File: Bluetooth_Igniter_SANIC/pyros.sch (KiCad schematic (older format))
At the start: 21 parts, among them J1 Screw_Terminal_01x02, J2 Screw_Terminal_01x02, J3 Screw_Terminal_01x02, Q3 Q_NMOS_GSD, Q4 Q_NMOS_GSD, U3 LTV-817S, U4 LTV-817S

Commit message: PCB Resizing
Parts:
- J1, J2, J3: footprint TerminalBlock_Phoenix:TerminalBlock_Phoenix_PT-1,5-2-5.0-H_1x02_P5.00mm_Horizontal -> iclrhw:PHOENIX_1757242
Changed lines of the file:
@@
 F 0 "J1" V 2772 3630 50  0000 L CNN
 F 1 "Screw_Terminal_01x02" V 2863 3630 50  0000 L CNN
-F 2 "TerminalBlock_Phoenix:TerminalBlock_Phoenix_PT-1,5-2-5.0-H_1x02_P5.00mm_Horizontal" H 2900 3550 50  0001 C CNN
+F 2 "iclrhw:PHOENIX_1757242" H 2900 3550 50  0001 C CNN
 F 3 "~" H 2900 3550 50  0001 C CNN
 	1    2900 3550
@@
 F 0 "J3" V 7422 3680 50  0000 L CNN
 F 1 "Screw_Terminal_01x02" V 7513 3680 50  0000 L CNN
-F 2 "TerminalBlock_Phoenix:TerminalBlock_Phoenix_PT-1,5-2-5.0-H_1x02_P5.00mm_Horizontal" H 7550 3600 50  0001 C CNN
+F 2 "iclrhw:PHOENIX_1757242" H 7550 3600 50  0001 C CNN
 F 3 "~" H 7550 3600 50  0001 C CNN
 	1    7550 3600
@@
 F 0 "J2" H 3480 1692 50  0000 L CNN
 F 1 "Screw_Terminal_01x02" H 3480 1601 50  0000 L CNN
-F 2 "TerminalBlock_Phoenix:TerminalBlock_Phoenix_PT-1,5-2-5.0-H_1x02_P5.00mm_Horizontal" H 3400 1700 50  0001 C CNN
+F 2 "iclrhw:PHOENIX_1757242" H 3400 1700 50  0001 C CNN
 F 3 "~" H 3400 1700 50  0001 C CNN
 	1    3400 1700

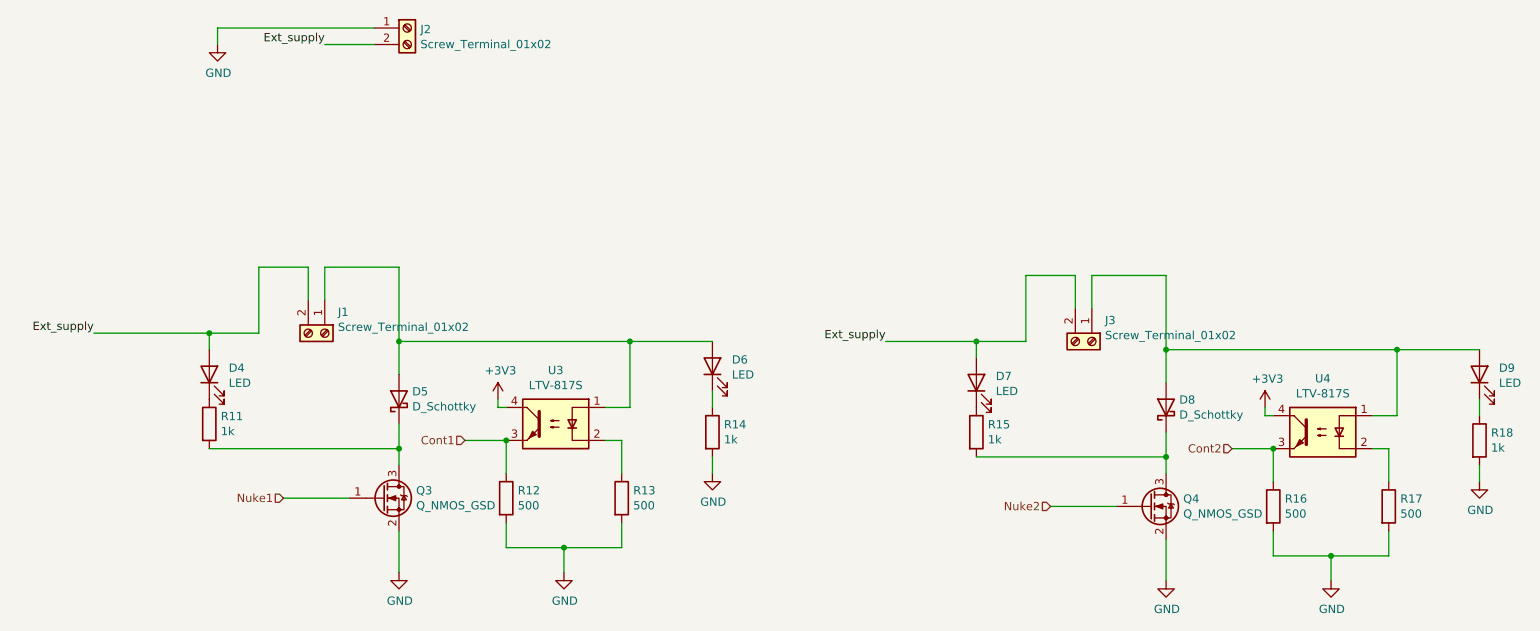
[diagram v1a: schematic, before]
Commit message: resized pcb
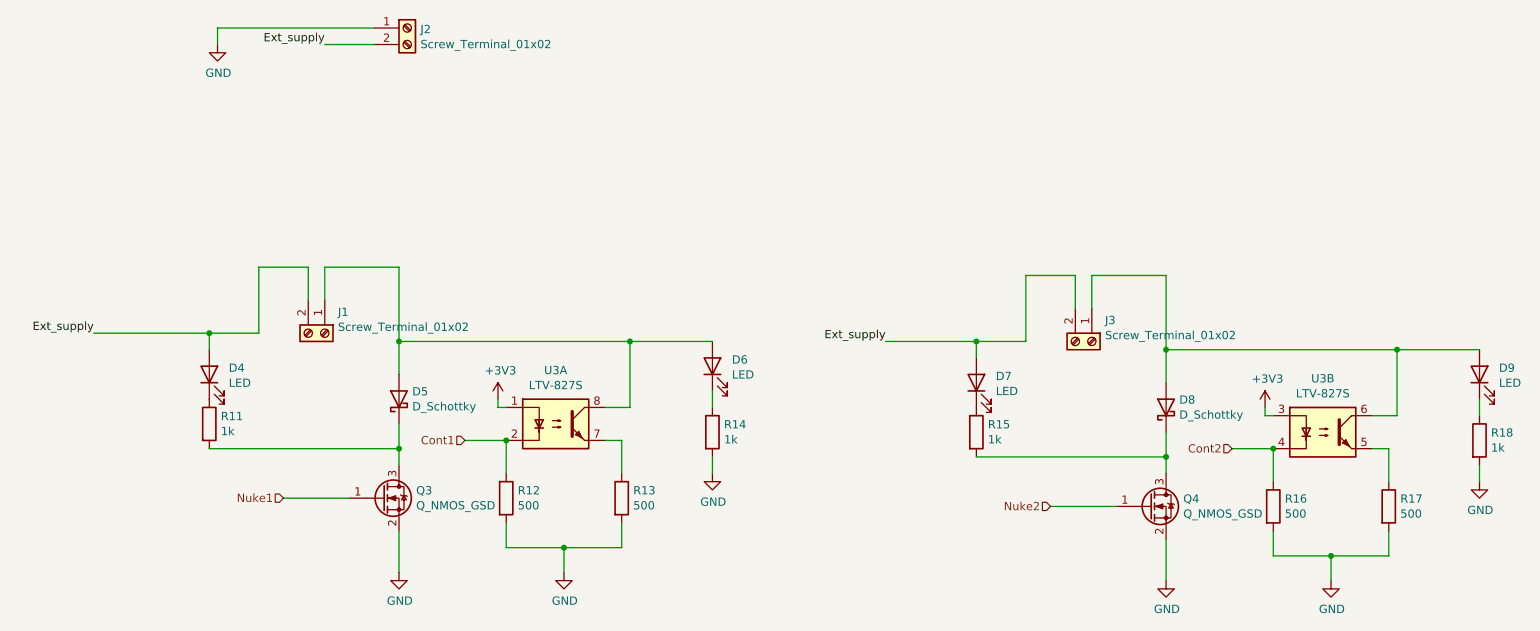
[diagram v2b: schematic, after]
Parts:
- removed U3, U4: LTV-817S, Package_DIP:SMDIP-4_W9.53mm, symbol Isolator:LTV-817S
- added U3: LTV-827S, Package_DIP:SMDIP-8_W9.53mm, symbol Isolator:LTV-827S
- J1, J2, J3: footprint iclrhw:PHOENIX_1757242 -> TerminalBlock_Phoenix:TerminalBlock_Phoenix_PT-1,5-2-5.0-H_1x02_P5.00mm_Horizontal
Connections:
- net +3V3: now also U3.1, U3.3
- net Cont1: now also U3.2
- net Cont2: now also U3.4
- net at D5.2 (A), D6.2 (A), J1.1 (Pin_1): now also U3.8
- net at R13.1: now also U3.7
- net at D8.2 (A), D9.2 (A), J3.1 (Pin_1): now also U3.6
- net at R17.1: now also U3.5
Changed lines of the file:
@@
 F 0 "J1" V 2772 3630 50  0000 L CNN
 F 1 "Screw_Terminal_01x02" V 2863 3630 50  0000 L CNN
-F 2 "iclrhw:PHOENIX_1757242" H 2900 3550 50  0001 C CNN
+F 2 "TerminalBlock_Phoenix:TerminalBlock_Phoenix_PT-1,5-2-5.0-H_1x02_P5.00mm_Horizontal" H 2900 3550 50  0001 C CNN
 F 3 "~" H 2900 3550 50  0001 C CNN
 	1    2900 3550
@@
 Wire Wire Line
 	4750 4000 4600 4000
-$Comp
-L Isolator:LTV-817S U3
-U 1 1 603B55A8
-P 4300 4100
-F 0 "U3" H 4300 4425 50  0000 C CNN
-F 1 "LTV-817S" H 4300 4334 50  0000 C CNN
-F 2 "Package_DIP:SMDIP-4_W9.53mm" H 4300 3800 50  0001 C CNN
-F 3 "http://www.us.liteon.com/downloads/LTV-817-827-847.PDF" H 3950 4400 50  0001 C CNN
-	1    4300 4100
-	-1   0    0    -1
-$EndComp
 Wire Wire Line
 	4000 4850 4000 4700
-Connection ~ 4000 4200
 Text HLabel 3750 4200 0    50   Input ~ 0
 Cont1
@@
 F 0 "J3" V 7422 3680 50  0000 L CNN
 F 1 "Screw_Terminal_01x02" V 7513 3680 50  0000 L CNN
-F 2 "iclrhw:PHOENIX_1757242" H 7550 3600 50  0001 C CNN
+F 2 "TerminalBlock_Phoenix:TerminalBlock_Phoenix_PT-1,5-2-5.0-H_1x02_P5.00mm_Horizontal" H 7550 3600 50  0001 C CNN
 F 3 "~" H 7550 3600 50  0001 C CNN
 	1    7550 3600
@@
 Wire Wire Line
 	9400 4050 9250 4050
-$Comp
-L Isolator:LTV-817S U4
-U 1 1 603DB582
-P 8950 4150
-F 0 "U4" H 8950 4475 50  0000 C CNN
-F 1 "LTV-817S" H 8950 4384 50  0000 C CNN
-F 2 "Package_DIP:SMDIP-4_W9.53mm" H 8950 3850 50  0001 C CNN
-F 3 "http://www.us.liteon.com/downloads/LTV-817-827-847.PDF" H 8600 4450 50  0001 C CNN
-	1    8950 4150
-	-1   0    0    -1
-$EndComp
 Wire Wire Line
 	8650 4900 8650 4750
-Connection ~ 8650 4250
 Text HLabel 8400 4250 0    50   Input ~ 0
 Cont2
@@
 F 0 "J2" H 3480 1692 50  0000 L CNN
 F 1 "Screw_Terminal_01x02" H 3480 1601 50  0000 L CNN
-F 2 "iclrhw:PHOENIX_1757242" H 3400 1700 50  0001 C CNN
+F 2 "TerminalBlock_Phoenix:TerminalBlock_Phoenix_PT-1,5-2-5.0-H_1x02_P5.00mm_Horizontal" H 3400 1700 50  0001 C CNN
 F 3 "~" H 3400 1700 50  0001 C CNN
 	1    3400 1700
@@
 	1    0    0    -1
 $EndComp
+$Comp
+L Isolator:LTV-827S U3
+U 1 1 60B943F7
+P 4300 4100
+F 0 "U3" H 4300 4425 50  0000 C CNN
+F 1 "LTV-827S" H 4300 4334 50  0000 C CNN
+F 2 "Package_DIP:SMDIP-8_W9.53mm" H 4300 3800 50  0001 C CNN
+F 3 "http://www.us.liteon.com/downloads/LTV-817-827-847.PDF" H 3500 4650 50  0001 C CNN
+	1    4300 4100
+	1    0    0    -1
+$EndComp
+$Comp
+L Isolator:LTV-827S U3
+U 2 1 60B94E21
+P 8950 4150
+F 0 "U3" H 8950 4475 50  0000 C CNN
+F 1 "LTV-827S" H 8950 4384 50  0000 C CNN
+F 2 "Package_DIP:SMDIP-8_W9.53mm" H 8950 3850 50  0001 C CNN
+F 3 "http://www.us.liteon.com/downloads/LTV-817-827-847.PDF" H 8150 4700 50  0001 C CNN
+	2    8950 4150
+	1    0    0    -1
+$EndComp
+Connection ~ 4000 4200
+Connection ~ 8650 4250
 $EndSCHEMATC
